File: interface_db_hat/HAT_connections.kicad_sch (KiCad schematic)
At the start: 12 parts, among them J1 GPIO, J5 Conn_01x04_Pin, U6 MCP23008-xSO

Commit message: lol
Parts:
- removed R1: 10k, Resistor_SMD:R_0603_1608Metric_Pad0.98x0.95mm_HandSolder, symbol Device:R_US
- added C4, C5: 100nF, symbol Device:C
- added R35, R36: 4.7k, Resistor_SMD:R_0603_1608Metric_Pad0.98x0.95mm_HandSolder, symbol Device:R_US
- added R6, R7, R8: 10k, Resistor_SMD:R_0603_1608Metric_Pad0.98x0.95mm_HandSolder, symbol Device:R_US
- added U2: TCA9617ADGKR, TCA9617:DGK0008A, symbol TCA9617:TCA9617ADGKR
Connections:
- net +3V3: now also C4.1, C5.1, R35.1, R36.1, R6.1, R7.1, R8.1, U2.1 (VCCA), U2.8 (VCCB)
- net GND: now also C4.2, C5.2, U2.4 (GND)
- net GPIO_13: now also J1.36 (Pin_36); no longer J1.38 (Pin_38)
- net I2C_SCL: now also R36.2, U2.2 (SCLA); no longer R64.1
- net I2C_SDA: now also R35.2, U2.3 (SDAA); no longer R63.1
- net GPA7 renamed I2CB_EN
- net I2CB_EN: now also U2.5 (EN)
- net PD_RST: no longer names the net of U6.6 (~{RESET})
- net PD_RST: now also R6.2; no longer J1.36 (Pin_36)
- new net GPIO_14: J1.38 (Pin_38)
- new net I2C_SCL_B: R64.1, R8.2, U2.7 (SCLB)
- new net I2C_SDA_B: R63.1, R7.2, U2.6 (SDAB)
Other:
- note added: "I2C buffer"
- moved on the sheet: D36, D37, D38, J1, J5, R62, R63, R64

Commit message: UPDATE
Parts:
- removed R62: 33, Resistor_SMD:R_0603_1608Metric_Pad0.98x0.95mm_HandSolder, symbol Device:R_US
- added D47, D48: TVS_3V3, Diode_SMD:D_0402_1005Metric_Pad0.77x0.64mm_HandSolder, symbol Device:D_Zener
- added J8: Conn_01x03_Pin, Connector_PinHeader_2.54mm:PinHeader_1x03_P2.54mm_Horizontal, symbol Connector:Conn_01x03_Pin
- added JP7: SolderJumper_2_Open, Jumper:SolderJumper-2_P1.3mm_Open_TrianglePad1.0x1.5mm, symbol Jumper:SolderJumper_2_Open
- added R39, R9: 10k, Resistor_SMD:R_0603_1608Metric_Pad0.98x0.95mm_HandSolder, symbol Device:R_US
- added R65, R66: 33, Resistor_SMD:R_0603_1608Metric_Pad0.98x0.95mm_HandSolder, symbol Device:R_US
- added U7: MCP23017x-x-SO, Package_SO:SOIC-28W_7.5x17.9mm_P1.27mm, symbol Interface_Expansion:MCP23017x-x-SO
- C4, C5: footprint (none) -> Capacitor_SMD:C_0603_1608Metric_Pad1.08x0.95mm_HandSolder
- D36, D37, D38: footprint Diode_SMD:D_0603_1608Metric_Pad1.05x0.95mm_HandSolder -> Diode_SMD:D_0402_1005Metric_Pad0.77x0.64mm_HandSolder
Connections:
- net +3V3: now also D36.1 (K), J5.2 (Pin_2), JP7.2 (B), R9.2, U7.9 (V_{DD})
- net EXP_INT: no longer J1.40 (Pin_40)
- net GND: now also D47.2 (A), D48.2 (A), J8.1 (Pin_1), R39.2, U7.10 (V_{SS}); no longer U6.9 (VSS)
- net GPA0: now also U7.21 (GPA0)
- net GPA1: now also U7.22 (GPA1)
- net GPA2: now also U7.23 (GPA2)
- net GPA3: now also U7.24 (GPA3)
- net GPA4: now also U7.25 (GPA4)
- net GPA5: now also U7.26 (GPA5)
- net GPA6: now also U7.27 (GPA6)
- net I2CB_EN: now also U7.28 (GPA7)
- net I2C_SCL: now also U7.12 (SCK)
- net I2C_SDA: now also U7.13 (SDA)
- net GPIO_13 renamed GPIO16
- net GPIO16: now also R9.1, U7.18 (~{RESET})
- net GPIO_14 renamed EXP_INT_A
- net EXP_INT_A: now also U7.20 (INTA)
- net RXDO renamed GPIO15/RXD0
- net GPIO15/RXD0: now also R66.1
- net TXDO renamed GPIO14/TXD0
- net GPIO14/TXD0: now also R65.1
- new net: D48.1 (K), J8.3 (Pin_3), R65.2
- new net: D47.1 (K), J8.2 (Pin_2), R66.2
- new net: U7.15 (A0), U7.16 (A1)
- new net: JP7.1 (A), R39.1, U7.17 (A2)
- new net EXP_INT_B: J1.40 (Pin_40), U7.19 (INTB)
- new net GPB0: U7.1 (GPB0)
- new net GPB1: U7.2 (GPB1)
- new net GPB2: U7.3 (GPB2)
- new net GPB3: U7.4 (GPB3)
- new net GPB4: U7.5 (GPB4)
- new net GPB5: U7.6 (GPB5)
- new net GPB6: U7.7 (GPB6)
- new net GPB7: U7.8 (GPB7)
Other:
- moved on the sheet: C4, C5, JP6, R35, R38, R6, U2, U6

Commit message: lol
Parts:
- removed JP6: SolderJumper_2_Open, Jumper:SolderJumper-2_P1.3mm_Open_TrianglePad1.0x1.5mm, symbol Jumper:SolderJumper_2_Open
- removed R38, R6: 10k, Resistor_SMD:R_0603_1608Metric_Pad0.98x0.95mm_HandSolder, symbol Device:R_US
- removed U6: MCP23008-xSO, Package_SO:SOIC-18W_7.5x11.6mm_P1.27mm, symbol Interface_Expansion:MCP23008-xSO
- added C6: 100nF, Capacitor_SMD:C_0603_1608Metric_Pad1.08x0.95mm_HandSolder, symbol Device:C
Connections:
- net +3V3: now also C6.2
- net GND: now also C6.1

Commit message: almomst done
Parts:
- removed R39: 10k, Resistor_SMD:R_0603_1608Metric_Pad0.98x0.95mm_HandSolder, symbol Device:R_US
- added JP8: SolderJumper_2_Open, Jumper:SolderJumper-2_P1.3mm_Open_TrianglePad1.0x1.5mm, symbol Jumper:SolderJumper_2_Open
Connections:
- net GPB7 is gone; now on net I2CB_EN: U7.8 (GPB7)
- net ADC1_CS: now also J1.26 (Pin_26); no longer J1.24 (Pin_24)
- net ADC2_CS: now also J1.24 (Pin_24); no longer J1.26 (Pin_26)
- net DAC1_CS: now also J1.15 (Pin_15); no longer J1.16 (Pin_16)
- net DAC2_CS: now also J1.13 (Pin_13); no longer J1.18 (Pin_18)
- net EXP_INT_A: now also J1.33 (Pin_33); no longer J1.38 (Pin_38)
- net EXP_INT_B: now also J1.31 (Pin_31); no longer J1.40 (Pin_40)
- net GND: now also U7.15 (A0), U7.16 (A1), JP8.2 (B)
- net GPIO_1: now also J1.18 (Pin_18); no longer J1.11 (Pin_11)
- net GPIO_11: now also J1.27 (Pin_27); no longer J1.28 (Pin_28)
- net GPIO_12: now also J1.36 (Pin_36); no longer J1.32 (Pin_32)
- net GPIO_2: now also J1.11 (Pin_11); no longer J1.13 (Pin_13)
- net GPIO_3: now also J1.16 (Pin_16); no longer J1.15 (Pin_15)
- net GPIO_4: now also J1.29 (Pin_29); no longer J1.27 (Pin_27)
- net GPIO_5: now also J1.28 (Pin_28); no longer J1.29 (Pin_29)
- net GPIO_6: now also J1.38 (Pin_38); no longer J1.31 (Pin_31)
- net GPIO_7: now also J1.40 (Pin_40); no longer J1.33 (Pin_33)
- net GPIO_8: now also J1.37 (Pin_37); no longer J1.35 (Pin_35)
- net GPIO_9: now also J1.35 (Pin_35); no longer J1.37 (Pin_37)
- net I2CB_EN: no longer U7.28 (GPA7)
- net at JP7.1 (A), U7.17 (A2): now also JP8.1 (A)
- net GPIO16 renamed GPIO12/PWM0
- net GPIO12/PWM0: now also J1.32 (Pin_32); no longer J1.36 (Pin_36)
- new net GPA7: U7.28 (GPA7)

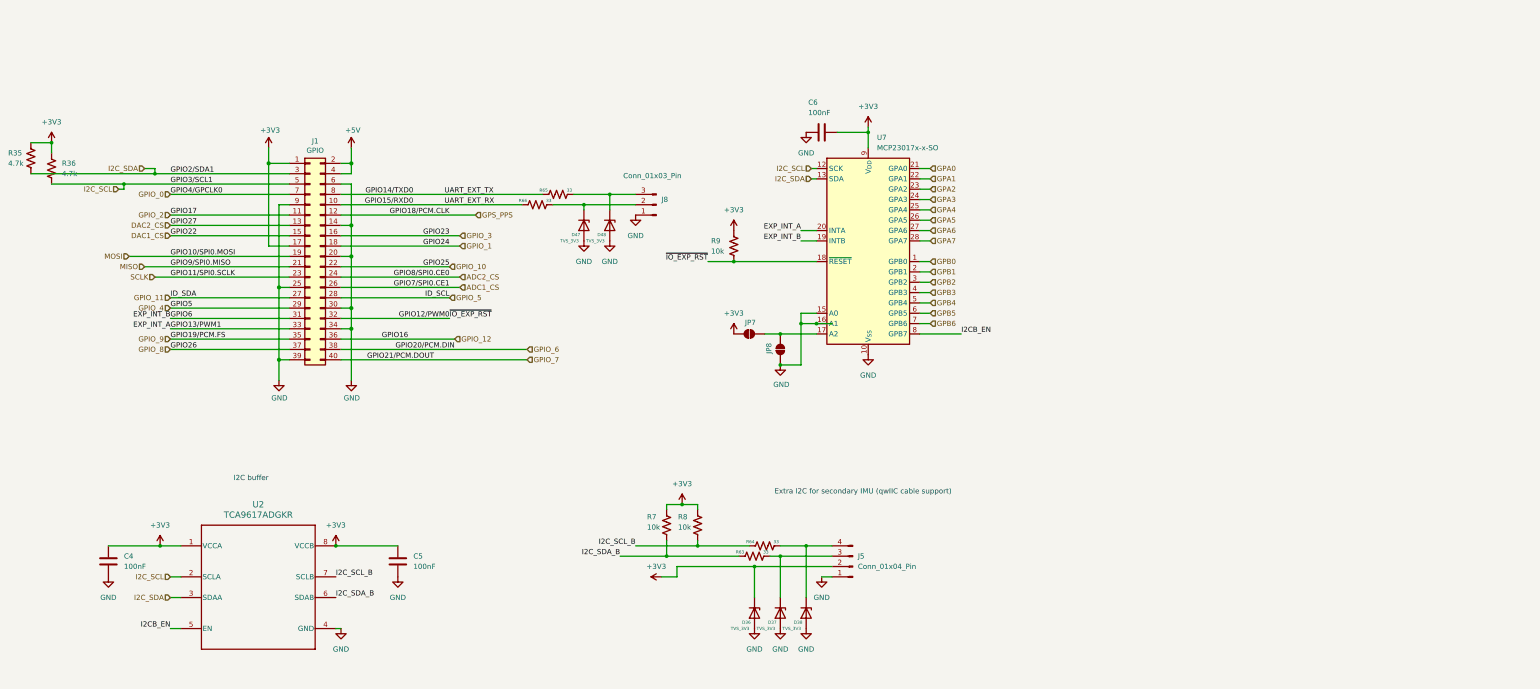
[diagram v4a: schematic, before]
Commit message: interface layout done
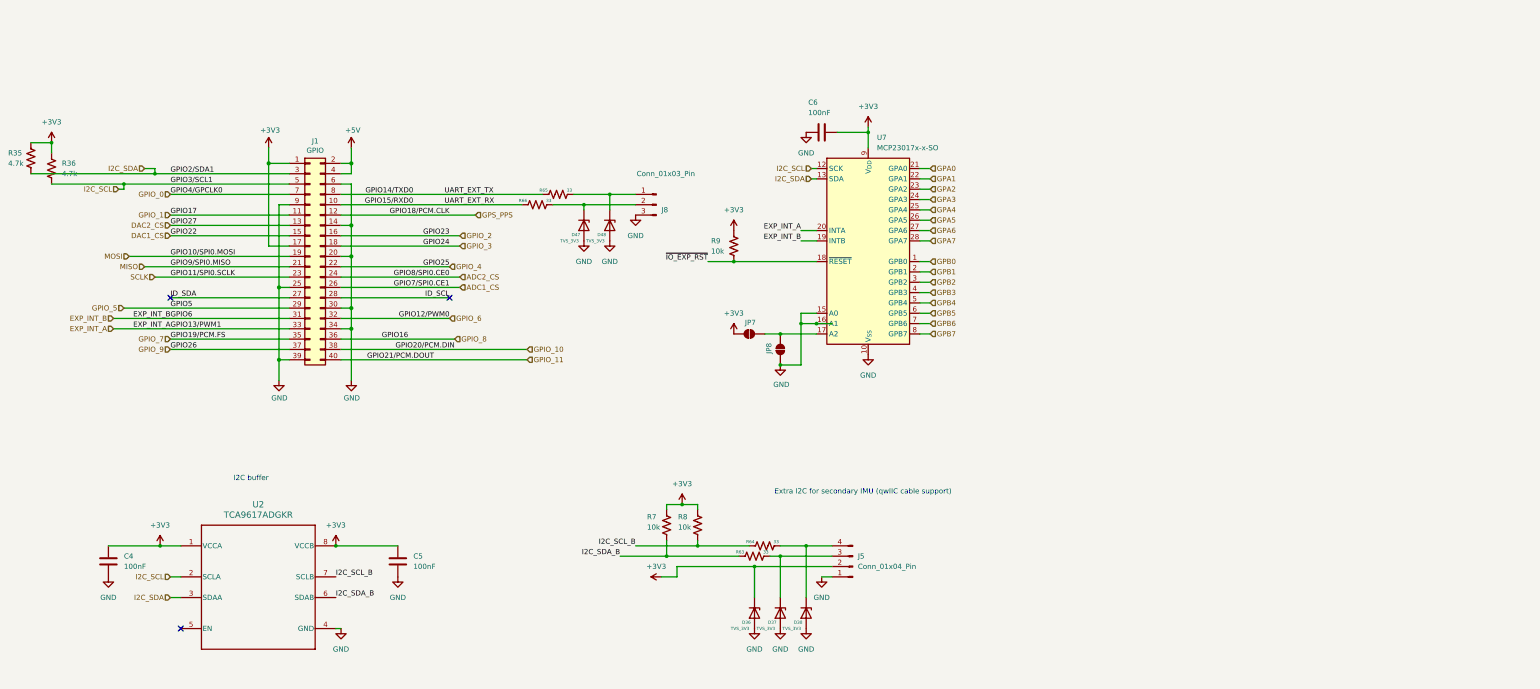
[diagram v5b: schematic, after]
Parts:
- D36, D37, D38, D47, D48: footprint Diode_SMD:D_0402_1005Metric_Pad0.77x0.64mm_HandSolder -> Diode_SMD:D_0603_1608Metric
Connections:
- net GPIO_12 is gone; now on net GPIO_8: J1.36 (Pin_36)
- net GND: now also J8.3 (Pin_3); no longer J8.1 (Pin_1)
- net GPIO_1: now also J1.11 (Pin_11); no longer J1.18 (Pin_18)
- net GPIO_10: now also J1.38 (Pin_38); no longer J1.22 (Pin_22)
- net GPIO_11: now also J1.40 (Pin_40); no longer J1.27 (Pin_27)
- net GPIO_2: now also J1.16 (Pin_16); no longer J1.11 (Pin_11)
- net GPIO_3: now also J1.18 (Pin_18); no longer J1.16 (Pin_16)
- net GPIO_4: now also J1.22 (Pin_22); no longer J1.29 (Pin_29)
- net GPIO_5: now also J1.29 (Pin_29); no longer J1.28 (Pin_28)
- net GPIO_6: now also J1.32 (Pin_32); no longer J1.38 (Pin_38)
- net GPIO_7: now also J1.35 (Pin_35); no longer J1.40 (Pin_40)
- net GPIO_8: no longer J1.37 (Pin_37)
- net GPIO_9: now also J1.37 (Pin_37); no longer J1.35 (Pin_35)
- net at D48.1 (K), R65.2: now also J8.1 (Pin_1); no longer J8.3 (Pin_3)
- net GPIO12/PWM0 renamed ~{IO_EXP_RST}
- net ~{IO_EXP_RST}: no longer J1.32 (Pin_32)
- net I2CB_EN: no longer names the net of U2.5 (EN)
- net I2CB_EN: no longer U7.8 (GPB7)
- new net GPB7: U7.8 (GPB7)
- new net ID_SCL: J1.28 (Pin_28)
- new net ID_SDA: J1.27 (Pin_27)
- no-connect marks 0 -> 3
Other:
- moved on the sheet: J8
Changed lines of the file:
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@@
 		(color 0 0 0 0)
 	)
+	(no_connect
+		(at 130.81 64.77)
+	)
+	(no_connect
+		(at 64.77 146.05)
+	)
+	(no_connect
+		(at 62.23 64.77)
+	)
 	(wire
 		(pts
@@
 	(wire
 		(pts
-			(xy 62.23 69.85) (xy 91.44 69.85)
-		)
-		(stroke
-			(width 0)
-			(type solid)
-		)
-	)
-	(wire
-		(pts
 			(xy 191.77 125.73) (xy 204.47 125.73)
 		)
@@
 	(wire
 		(pts
-			(xy 62.23 146.05) (xy 64.77 146.05)
-		)
-		(stroke
-			(width 0)
-			(type default)
-		)
-	)
-	(wire
-		(pts
 			(xy 50.8 36.83) (xy 91.44 36.83)
 		)
@@
 	(wire
 		(pts
+			(xy 246.38 73.66) (xy 248.92 73.66)
+		)
+		(stroke
+			(width 0)
+			(type default)
+		)
+	)
+	(wire
+		(pts
 			(xy 55.88 33.02) (xy 58.42 33.02)
 		)
@@
 	(wire
 		(pts
-			(xy 246.38 48.26) (xy 248.92 48.26)
+			(xy 48.26 72.39) (xy 91.44 72.39)
 		)
 		(stroke
@@
 	(wire
 		(pts
-			(xy 106.68 27.94) (xy 106.68 31.75)
+			(xy 246.38 48.26) (xy 248.92 48.26)
 		)
 		(stroke
 			(width 0)
-			(type solid)
+			(type default)
 		)
 	)
 	(wire
 		(pts
-			(xy 218.44 138.43) (xy 218.44 125.73)
+			(xy 106.68 27.94) (xy 106.68 31.75)
 		)
 		(stroke
 			(width 0)
-			(type default)
+			(type solid)
 		)
 	)
 	(wire
 		(pts
-			(xy 246.38 73.66) (xy 256.54 73.66)
+			(xy 218.44 138.43) (xy 218.44 125.73)
 		)
 		(stroke
@@
 	(wire
 		(pts
-			(xy 91.44 72.39) (xy 62.23 72.39)
-		)
-		(stroke
-			(width 0)
-			(type solid)
-		)
-	)
-	(wire
-		(pts
 			(xy 104.14 64.77) (xy 130.81 64.77)
 		)
@@
 	(wire
 		(pts
+			(xy 48.26 69.85) (xy 91.44 69.85)
+		)
+		(stroke
+			(width 0)
+			(type default)
+		)
+	)
+	(wire
+		(pts
 			(xy 86.36 31.75) (xy 91.44 31.75)
 		)
@@
 	(wire
 		(pts
-			(xy 62.23 67.31) (xy 91.44 67.31)
+			(xy 50.8 67.31) (xy 91.44 67.31)
 		)
 		(stroke
@@
 		)
 	)
-	(label "I2CB_EN"
-		(at 62.23 146.05 180)
-		(effects
-			(font
-				(size 1.27 1.27)
-			)
-			(justify right bottom)
-		)
-	)
 	(label "GPIO2{slash}SDA1"
 		(at 62.23 34.29 0)
@@
 		)
 	)
-	(label "~{IO_EXP_RST}"
-		(at 130.81 69.85 0)
-		(effects
-			(font
-				(size 1.27 1.27)
-			)
-			(justify left bottom)
-		)
-	)
 	(label "GPIO13{slash}PWM1"
 		(at 62.23 72.39 0)
@@
 		)
 	)
-	(label "I2CB_EN"
-		(at 256.54 73.66 0)
+	(label "GPIO21{slash}PCM.DOUT"
+		(at 127 80.01 180)
 		(effects
 			(font
 				(size 1.27 1.27)
 			)
-			(justify left bottom)
+			(justify right bottom)
 		)
 	)
-	(label "GPIO21{slash}PCM.DOUT"
-		(at 127 80.01 180)
+	(hierarchical_label "GPIO_4"
+		(shape input)
+		(at 130.81 57.15 0)
 		(effects
 			(font
 				(size 1.27 1.27)
 			)
-			(justify right bottom)
+			(justify left)
 		)
 	)
@@
 		)
 	)
+	(hierarchical_label "GPIO_6"
+		(shape input)
+		(at 130.81 69.85 0)
+		(effects
+			(font
+				(size 1.27 1.27)
+			)
+			(justify left)
+		)
+	)
 	(hierarchical_label "GPA2"
 		(shape input)
@@
 		)
 	)
+	(hierarchical_label "GPIO_11"
+		(shape input)
+		(at 149.86 80.01 0)
+		(effects
+			(font
+				(size 1.27 1.27)
+			)
+			(justify left)
+		)
+	)
+	(hierarchical_label "EXP_INT_B"
+		(shape input)
+		(at 48.26 69.85 180)
+		(effects
+			(font
+				(size 1.27 1.27)
+			)
+			(justify right)
+		)
+	)
 	(hierarchical_label "ADC1_CS"
 		(shape input)
@@
 		)
 	)
-	(hierarchical_label "GPA7"
+	(hierarchical_label "GPIO_3"
 		(shape input)
-		(at 248.92 50.8 0)
+		(at 133.35 52.07 0)
 		(effects
 			(font
@@
 		)
 	)
-	(hierarchical_label "GPA5"
+	(hierarchical_label "GPA7"
 		(shape input)
-		(at 248.92 45.72 0)
+		(at 248.92 50.8 0)
 		(effects
 			(font
@@
 		)
 	)
-	(hierarchical_label "GPB2"
+	(hierarchical_label "GPA5"
 		(shape input)
-		(at 248.92 60.96 0)
+		(at 248.92 45.72 0)
 		(effects
 			(font
@@
 		)
 	)
-	(hierarchical_label "GPIO_3"
+	(hierarchical_label "GPB2"
 		(shape input)
-		(at 133.35 49.53 0)
+		(at 248.92 60.96 0)
 		(effects
 			(font
@@
 		)
 	)
-	(hierarchical_label "GPIO_6"
-		(shape input)
-		(at 149.86 77.47 0)
-		(effects
-			(font
-				(size 1.27 1.27)
-			)
-			(justify left)
-		)
-	)
-	(hierarchical_label "GPIO_12"
+	(hierarchical_label "GPIO_2"
 		(shape input)
-		(at 132.08 74.93 0)
+		(at 133.35 49.53 0)
 		(effects
 			(font
@@
 		)
 	)
-	(hierarchical_label "GPIO_4"
+	(hierarchical_label "GPIO_5"
 		(shape input)
-		(at 62.23 67.31 180)
+		(at 50.8 67.31 180)
 		(effects
 			(font
@@
 		)
 	)
-	(hierarchical_label "GPIO_11"
-		(shape input)
-		(at 62.23 64.77 180)
-		(effects
-			(font
-				(size 1.27 1.27)
-			)
-			(justify right)
-		)
-	)
 	(hierarchical_label "GPB5"
 		(shape input)
@@
 		)
 	)
-	(hierarchical_label "GPIO_10"
-		(shape input)
-		(at 130.81 57.15 0)
-		(effects
-			(font
-				(size 1.27 1.27)
-			)
-			(justify left)
-		)
-	)
-	(hierarchical_label "GPIO_9"
+	(hierarchical_label "EXP_INT_A"
 		(shape input)
-		(at 62.23 74.93 180)
+		(at 48.26 72.39 180)
 		(effects
 			(font
@@
 		)
 	)
-	(hierarchical_label "GPIO_1"
-		(shape input)
-		(at 133.35 52.07 0)
-		(effects
-			(font
-				(size 1.27 1.27)
-			)
-			(justify left)
-		)
-	)
 	(hierarchical_label "GPS_PPS"
 		(shape input)
@@
 		)
 	)
-	(hierarchical_label "GPIO_7"
+	(hierarchical_label "GPB7"
 		(shape input)
-		(at 149.86 80.01 0)
+		(at 248.92 73.66 0)
 		(effects
 			(font
@@
 		)
 	)
-	(hierarchical_label "GPIO_8"
+	(hierarchical_label "GPIO_9"
 		(shape input)
 		(at 62.23 77.47 180)
@@
 		)
 	)
-	(hierarchical_label "GPIO_5"
+	(hierarchical_label "GPIO_7"
 		(shape input)
-		(at 130.81 64.77 0)
+		(at 62.23 74.93 180)
 		(effects
 			(font
 				(size 1.27 1.27)
 			)
-			(justify left)
+			(justify right)
 		)
 	)
@@
 		)
 	)
+	(hierarchical_label "GPIO_10"
+		(shape input)
+		(at 149.86 77.47 0)
+		(effects
+			(font
+				(size 1.27 1.27)
+			)
+			(justify left)
+		)
+	)
 	(hierarchical_label "GPB1"
 		(shape input)
@@
 		)
 	)
-	(hierarchical_label "GPIO_2"
+	(hierarchical_label "GPIO_1"
 		(shape input)
 		(at 62.23 44.45 180)
@@
 		)
 	)
+	(hierarchical_label "GPIO_8"
+		(shape input)
+		(at 132.08 74.93 0)
+		(effects
+			(font
+				(size 1.27 1.27)
+			)
+			(justify left)
+		)
+	)
 	(hierarchical_label "MISO"
 		(shape input)
@@
 			)
 		)
-		(property "Footprint" "Diode_SMD:D_0402_1005Metric_Pad0.77x0.64mm_HandSolder"
+		(property "Footprint" "Diode_SMD:D_0603_1608Metric"
 			(at 170.18 46.99 0)
 			(hide yes)
@@
 			)
 		)
-		(property "Footprint" "Diode_SMD:D_0402_1005Metric_Pad0.77x0.64mm_HandSolder"
+		(property "Footprint" "Diode_SMD:D_0603_1608Metric"
 			(at 218.44 142.24 0)
 			(hide yes)
@@
 			)
 		)
-		(property "Footprint" "Diode_SMD:D_0402_1005Metric_Pad0.77x0.64mm_HandSolder"
+		(property "Footprint" "Diode_SMD:D_0603_1608Metric"
 			(at 212.09 142.24 0)
 			(hide yes)
@@
 			)
 		)
-		(property "Footprint" "Diode_SMD:D_0402_1005Metric_Pad0.77x0.64mm_HandSolder"
+		(property "Footprint" "Diode_SMD:D_0603_1608Metric"
 			(at 205.74 142.24 0)
 			(hide yes)
@@
 			)
 		)
-		(property "Footprint" "Diode_SMD:D_0402_1005Metric_Pad0.77x0.64mm_HandSolder"
+		(property "Footprint" "Diode_SMD:D_0603_1608Metric"
 			(at 163.83 46.99 0)
 			(hide yes)
@@
 	(symbol
 		(lib_id "Connector:Conn_01x03_Pin")
-		(at 181.61 41.91 180)
+		(at 181.61 41.91 0)
+		(mirror y)
 		(unit 1)
 		(body_style 1)
@@
 		(dnp no)
 		(property "Reference" "J8"
-			(at 182.88 40.6399 0)
+			(at 182.88 43.1801 0)
 			(show_name no)
 			(do_not_autoplace no)
@@
 		)
 		(property "Value" "Conn_01x03_Pin"
-			(at 173.482 34.798 0)
+			(at 176.784 34.29 0)
 			(show_name no)
 			(do_not_autoplace no)

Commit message: fixed interface schematic
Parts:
- removed C4: 100nF, Capacitor_SMD:C_0603_1608Metric_Pad1.08x0.95mm_HandSolder, symbol Device:C
- removed JP8: SolderJumper_2_Open, Jumper:SolderJumper-2_P1.3mm_Open_TrianglePad1.0x1.5mm, symbol Jumper:SolderJumper_2_Open
- added R13: 10k, Resistor_SMD:R_0603_1608Metric_Pad0.98x0.95mm_HandSolder, symbol Device:R_US
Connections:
- net ADC1_CS is gone; now on net GPIO_8: J1.26 (Pin_26)
- net ADC2_CS is gone; now on net GPIO_7: J1.24 (Pin_24)
- net DAC1_CS is gone; now on net GPIO_3: J1.15 (Pin_15)
- net DAC2_CS is gone; now on net GPIO_2: J1.13 (Pin_13)
- net GND: now also R13.1
- net GPIO_11: now also J1.32 (Pin_32); no longer J1.40 (Pin_40)
- net GPIO_2: no longer J1.16 (Pin_16)
- net GPIO_3: no longer J1.18 (Pin_18)
- net GPIO_4: now also J1.16 (Pin_16); no longer J1.22 (Pin_22)
- net GPIO_5: now also J1.18 (Pin_18); no longer J1.29 (Pin_29)
- net GPIO_6: now also J1.22 (Pin_22); no longer J1.32 (Pin_32)
- net GPIO_7: no longer J1.35 (Pin_35)
- net GPIO_8: no longer J1.36 (Pin_36)
- net GPIO_9: now also J1.29 (Pin_29); no longer J1.37 (Pin_37)
- net at JP7.1 (A), U7.17 (A2): now also R13.2
- net GPIO_10 renamed GPIO_16
- new net GPIO_13: J1.35 (Pin_35)
- new net GPIO_14: J1.36 (Pin_36)
- new net GPIO_15: J1.37 (Pin_37)
- new net GPIO_17: J1.40 (Pin_40)
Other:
- moved on the sheet: C5
